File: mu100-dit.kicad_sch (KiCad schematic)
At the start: 6 parts, among them J1 Conn_01x05_Male, J2 Conn_01x02_Male, U1 TOTX-177L, U2 AK4103A

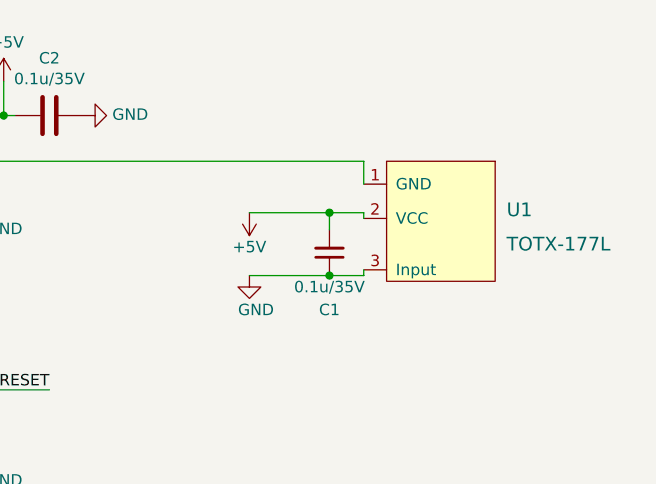
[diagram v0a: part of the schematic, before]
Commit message: fix issue with totx177 footprint, fix schematics
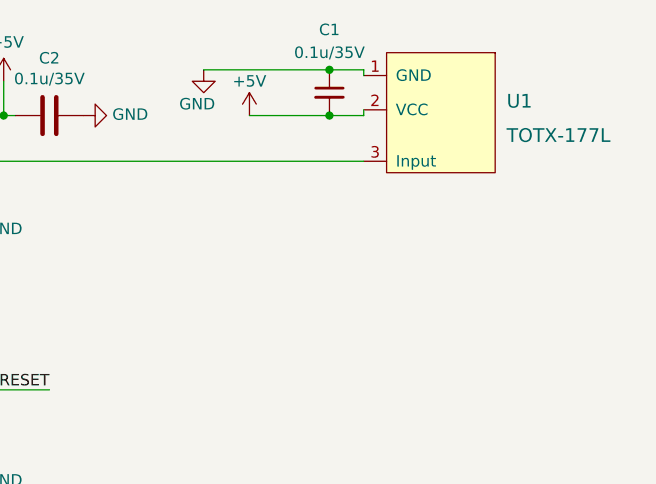
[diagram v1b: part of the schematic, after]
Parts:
- C1, C2: footprint Capacitor_SMD:C_0603_1608Metric -> Capacitor_SMD:C_0805_2012Metric_Pad1.18x1.45mm_HandSolder
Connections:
- net GND: now also U1.1 (GND); no longer U1.3 (Input)
- net TXP: now also U1.3 (Input); no longer U1.1 (GND)
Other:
- moved on the sheet: C1, U1
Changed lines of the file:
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@@
   (junction (at 173.99 95.25) (diameter 0) (color 0 0 0 0)
   )
-  (junction (at 210.185 106.045) (diameter 0) (color 0 0 0 0)
-  )
-  (junction (at 210.185 113.03) (diameter 0) (color 0 0 0 0)
+  (junction (at 210.185 95.25) (diameter 0) (color 0 0 0 0)
+  )
+  (junction (at 210.185 90.17) (diameter 0) (color 0 0 0 0)
   )
   (no_connect (at 133.35 135.89))
@@
   (no_connect (at 168.91 130.81))
   (no_connect (at 168.91 102.87))
-  (wire (pts (xy 213.995 113.03) (xy 213.995 112.395))
-    (stroke (width 0) (type default) (color 0 0 0 0))
-  )
-  (wire (pts (xy 210.185 106.045) (xy 201.295 106.045))
-    (stroke (width 0) (type default) (color 0 0 0 0))
-  )
-  (wire (pts (xy 210.185 113.03) (xy 213.995 113.03))
+  (wire (pts (xy 213.995 90.17) (xy 213.995 90.805))
+    (stroke (width 0) (type default) (color 0 0 0 0))
+  )
+  (wire (pts (xy 210.185 95.25) (xy 201.295 95.25))
+    (stroke (width 0) (type default) (color 0 0 0 0))
+  )
+  (wire (pts (xy 210.185 90.17) (xy 213.995 90.17))
     (stroke (width 0) (type default) (color 0 0 0 0))
   )
@@
     (stroke (width 0) (type default) (color 0 0 0 0))
   )
-  (wire (pts (xy 201.295 113.03) (xy 210.185 113.03))
+  (wire (pts (xy 196.215 90.17) (xy 210.185 90.17))
     (stroke (width 0) (type default) (color 0 0 0 0))
   )
@@
     (stroke (width 0) (type solid) (color 0 0 0 0))
   )
-  (wire (pts (xy 210.185 106.045) (xy 210.185 107.95))
-    (stroke (width 0) (type default) (color 0 0 0 0))
-  )
   (wire (pts (xy 40.64 116.84) (xy 40.64 118.11))
     (stroke (width 0) (type solid) (color 0 0 0 0))
@@
     (stroke (width 0) (type solid) (color 0 0 0 0))
   )
-  (wire (pts (xy 213.995 106.045) (xy 210.185 106.045))
+  (wire (pts (xy 213.995 95.25) (xy 210.185 95.25))
     (stroke (width 0) (type default) (color 0 0 0 0))
   )
@@
     (stroke (width 0) (type default) (color 0 0 0 0))
   )
-  (wire (pts (xy 213.995 100.33) (xy 213.995 102.87))
-    (stroke (width 0) (type default) (color 0 0 0 0))
-  )
   (wire (pts (xy 40.64 120.65) (xy 40.64 121.92))
     (stroke (width 0) (type solid) (color 0 0 0 0))
@@
     (stroke (width 0) (type solid) (color 0 0 0 0))
   )
-  (wire (pts (xy 213.995 106.045) (xy 213.995 106.68))
+  (wire (pts (xy 213.995 95.25) (xy 213.995 94.615))
     (stroke (width 0) (type default) (color 0 0 0 0))
   )
@@
     (pin "1")
   )
-  (symbol (lib_id "power:GND") (at 201.295 113.03 0) (mirror y) (unit 1)
-    (in_bom yes) (on_board yes)
-    (property "Reference" "#PWR0102" (id 0) (at 201.295 119.38 0)
-      (effects (font (size 1.27 1.27)) hide)
-    )
-    (property "Value" "GND" (id 1) (at 200.025 116.84 0)
-      (effects (font (size 1.27 1.27)) (justify right))
-    )
-    (property "Footprint" "" (id 2) (at 201.295 113.03 0)
-      (effects (font (size 1.27 1.27)) hide)
-    )
-    (property "Datasheet" "" (id 3) (at 201.295 113.03 0)
-      (effects (font (size 1.27 1.27)) hide)
-    )
-    (pin "1")
-  )
-  (symbol (lib_id "power:+5V") (at 201.295 106.045 0) (mirror x) (unit 1)
-    (in_bom yes) (on_board yes)
-    (property "Reference" "#PWR0101" (id 0) (at 201.295 102.235 0)
-      (effects (font (size 1.27 1.27)) hide)
-    )
-    (property "Value" "+5V" (id 1) (at 201.295 109.855 0))
-    (property "Footprint" "" (id 2) (at 201.295 106.045 0)
-      (effects (font (size 1.27 1.27)) hide)
-    )
-    (property "Datasheet" "" (id 3) (at 201.295 106.045 0)
-      (effects (font (size 1.27 1.27)) hide)
-    )
-    (pin "1")
-  )
-  (symbol (lib_id "Device:C_Small") (at 210.185 110.49 0) (mirror x) (unit 1)
-    (in_bom yes) (on_board yes)
-    (property "Reference" "C1" (id 0) (at 210.185 116.84 0))
-    (property "Value" "0.1u/35V" (id 1) (at 210.185 114.3 0))
-    (property "Footprint" "Capacitor_SMD:C_0603_1608Metric" (id 2) (at 210.185 110.49 0)
-      (effects (font (size 1.27 1.27)) hide)
-    )
-    (property "Datasheet" "~" (id 3) (at 210.185 110.49 0)
+  (symbol (lib_id "power:GND") (at 196.215 90.17 0) (unit 1)
+    (in_bom yes) (on_board yes)
+    (property "Reference" "#PWR0102" (id 0) (at 196.215 96.52 0)
+      (effects (font (size 1.27 1.27)) hide)
+    )
+    (property "Value" "GND" (id 1) (at 197.485 93.98 0)
+      (effects (font (size 1.27 1.27)) (justify right))
+    )
+    (property "Footprint" "" (id 2) (at 196.215 90.17 0)
+      (effects (font (size 1.27 1.27)) hide)
+    )
+    (property "Datasheet" "" (id 3) (at 196.215 90.17 0)
+      (effects (font (size 1.27 1.27)) hide)
+    )
+    (pin "1")
+  )
+  (symbol (lib_id "power:+5V") (at 201.295 95.25 0) (unit 1)
+    (in_bom yes) (on_board yes)
+    (property "Reference" "#PWR0101" (id 0) (at 201.295 99.06 0)
+      (effects (font (size 1.27 1.27)) hide)
+    )
+    (property "Value" "+5V" (id 1) (at 201.295 91.44 0))
+    (property "Footprint" "" (id 2) (at 201.295 95.25 0)
+      (effects (font (size 1.27 1.27)) hide)
+    )
+    (property "Datasheet" "" (id 3) (at 201.295 95.25 0)
+      (effects (font (size 1.27 1.27)) hide)
+    )
+    (pin "1")
+  )
+  (symbol (lib_id "Device:C_Small") (at 210.185 92.71 0) (unit 1)
+    (in_bom yes) (on_board yes)
+    (property "Reference" "C1" (id 0) (at 210.185 85.725 0))
+    (property "Value" "0.1u/35V" (id 1) (at 210.185 88.265 0))
+    (property "Footprint" "Capacitor_SMD:C_0805_2012Metric_Pad1.18x1.45mm_HandSolder" (id 2) (at 210.185 92.71 0)
+      (effects (font (size 1.27 1.27)) hide)
+    )
+    (property "Datasheet" "~" (id 3) (at 210.185 92.71 0)
       (effects (font (size 1.27 1.27)) hide)
     )
@@
     (pin "1")
   )
-  (symbol (lib_id "selfmade:totx177") (at 222.885 106.045 0) (mirror y) (unit 1)
+  (symbol (lib_id "selfmade:totx177") (at 222.885 93.98 0) (mirror y) (unit 1)
     (in_bom yes) (on_board yes) (fields_autoplaced)
-    (property "Reference" "U1" (id 0) (at 229.87 105.7275 0)
+    (property "Reference" "U1" (id 0) (at 229.87 93.6625 0)
       (effects (font (size 1.524 1.524)) (justify right))
     )
-    (property "Value" "TOTX-177L" (id 1) (at 229.87 109.5375 0)
+    (property "Value" "TOTX-177L" (id 1) (at 229.87 97.4725 0)
       (effects (font (size 1.524 1.524)) (justify right))
     )
-    (property "Footprint" "footprints:Toshiba_TOTX177" (id 2) (at 224.155 104.14 0)
+    (property "Footprint" "footprints:Toshiba_TOTX177" (id 2) (at 224.155 92.075 0)
       (effects (font (size 1.524 1.524)) hide)
     )
-    (property "Datasheet" "" (id 3) (at 224.155 104.14 0)
+    (property "Datasheet" "" (id 3) (at 224.155 92.075 0)
       (effects (font (size 1.524 1.524)) hide)
     )
@@
     (property "Reference" "C2" (id 0) (at 179.07 88.8808 90))
     (property "Value" "0.1u/35V" (id 1) (at 179.07 91.1795 90))
-    (property "Footprint" "Capacitor_SMD:C_0603_1608Metric" (id 2) (at 175.26 96.2152 0)
+    (property "Footprint" "Capacitor_SMD:C_0805_2012Metric_Pad1.18x1.45mm_HandSolder" (id 2) (at 175.26 96.2152 0)
       (effects (font (size 1.27 1.27)) hide)
     )
@@
     )
     (path "/5c8001ed-df23-4c03-bf06-383745b6e880"
-      (reference "C1") (unit 1) (value "0.1u/35V") (footprint "Capacitor_SMD:C_0603_1608Metric")
+      (reference "C1") (unit 1) (value "0.1u/35V") (footprint "Capacitor_SMD:C_0805_2012Metric_Pad1.18x1.45mm_HandSolder")
     )
     (path "/94bc1406-7b89-4767-b44d-59c48e810678"
-      (reference "C2") (unit 1) (value "0.1u/35V") (footprint "Capacitor_SMD:C_0603_1608Metric")
+      (reference "C2") (unit 1) (value "0.1u/35V") (footprint "Capacitor_SMD:C_0805_2012Metric_Pad1.18x1.45mm_HandSolder")
     )
     (path "/ff659391-c1b5-4db7-a75c-a813fac59ee3"

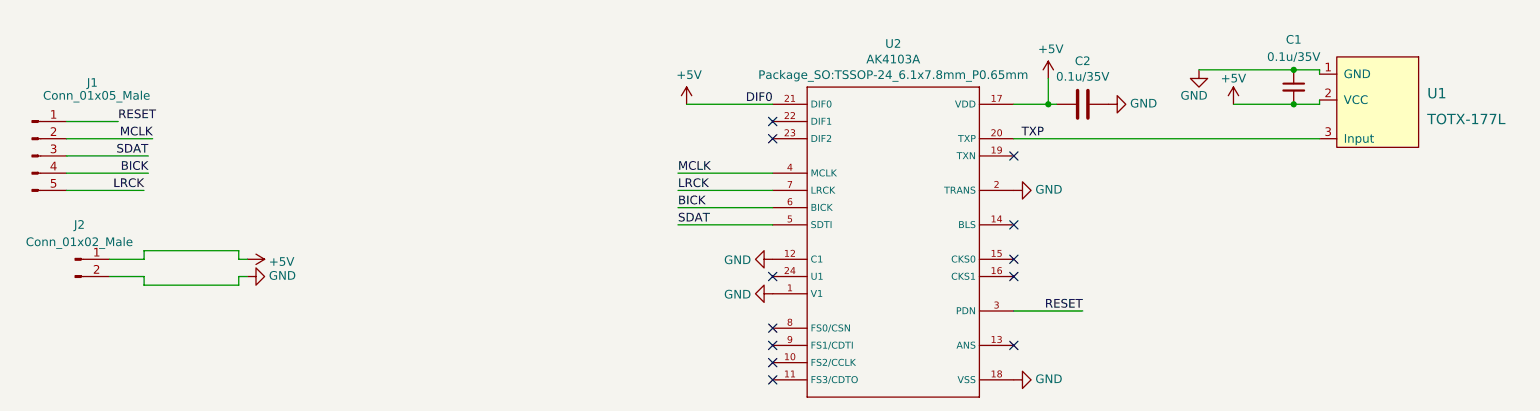
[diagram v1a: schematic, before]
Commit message: add jumpers to board
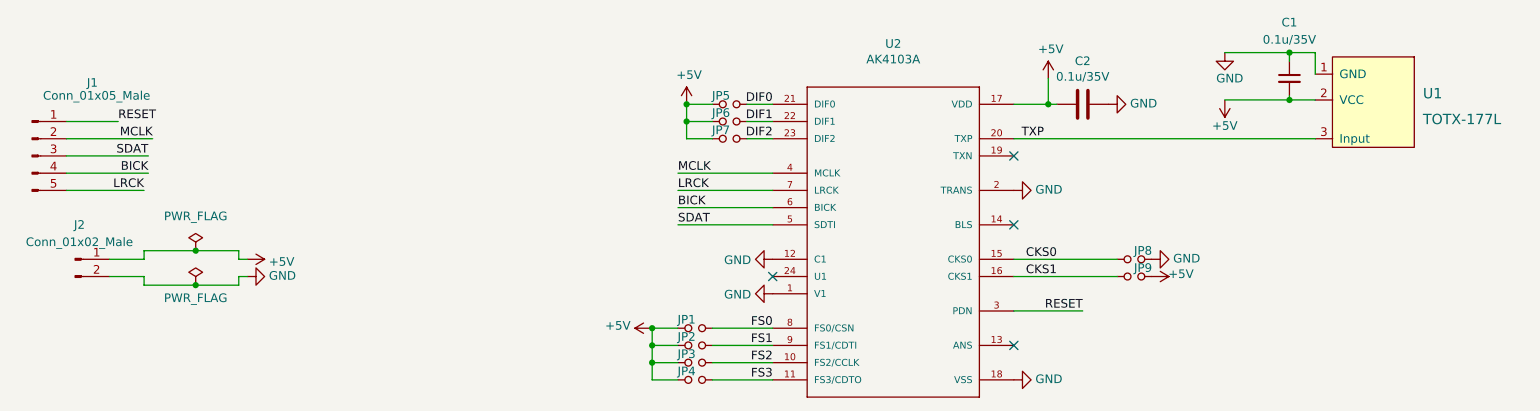
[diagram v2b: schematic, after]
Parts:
- added JP1, JP2, JP3, JP4, JP5, JP6, JP7, JP8, JP9: Jumper_NO_Small, Capacitor_SMD:C_0402_1005Metric_Pad0.74x0.62mm_HandSolder, symbol Device:Jumper_NO_Small
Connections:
- net +5V: now also JP1.1, JP2.1, JP3.1, JP4.1, JP5.1, JP6.1, JP7.1, JP9.1; no longer U2.21 (DIF0)
- net GND: now also JP8.1
- net FS2: now reaches U2.10 (FS2/CCLK)
- net FS2: now also JP3.2
- net FS3: now reaches U2.11 (FS3/CDTO)
- net FS3: now also JP4.2
- net CKS0: now reaches U2.15 (CKS0)
- net CKS0: now also JP8.2
- net CKS1: now reaches U2.16 (CKS1)
- net CKS1: now also JP9.2
- net DIF1: now reaches U2.22 (DIF1)
- net DIF1: now also JP6.2
- net DIF2: now reaches U2.23 (DIF2)
- net DIF2: now also JP7.2
- net FS0: now reaches U2.8 (FS0/CSN)
- net FS0: now also JP1.2
- net FS1: now reaches U2.9 (FS1/CDTI)
- net FS1: now also JP2.2
- new net DIF0: JP5.2, U2.21 (DIF0)
- no-connect marks 12 -> 4
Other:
- moved on the sheet: U1
